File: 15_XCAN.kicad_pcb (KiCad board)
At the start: 2 copper layers, 12.1 x 17.1 mm, 5 parts, among them J1 Conn_01x06, J7 Conn_01x01, U1 MCP2551-I-SN

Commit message: maj fichiers de fabrication
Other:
- rule pad_to_mask_clearance: 0.05 -> 0
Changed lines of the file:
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@@
   )
   (setup
-    (pad_to_mask_clearance 0.05)
+    (stackup
+      (layer "F.SilkS" (type "Top Silk Screen"))
+      (layer "F.Paste" (type "Top Solder Paste"))
+      (layer "F.Mask" (type "Top Solder Mask") (thickness 0.01))
+      (layer "F.Cu" (type "copper") (thickness 0.035))
+      (layer "dielectric 1" (type "core") (thickness 1.51) (material "FR4") (epsilon_r 4.5) (loss_tangent 0.02))
+      (layer "B.Cu" (type "copper") (thickness 0.035))
+      (layer "B.Mask" (type "Bottom Solder Mask") (thickness 0.01))
+      (layer "B.Paste" (type "Bottom Solder Paste"))
+      (layer "B.SilkS" (type "Bottom Silk Screen"))
+      (copper_finish "None")
+      (dielectric_constraints no)
+    )
+    (pad_to_mask_clearance 0)
     (grid_origin 104.14 78.74)
     (pcbplotparams
       (layerselection 0x00310fc_ffffffff)
       (disableapertmacros false)
-      (usegerberextensions false)
-      (usegerberattributes true)
-      (usegerberadvancedattributes true)
+      (usegerberextensions true)
+      (usegerberattributes false)
+      (usegerberadvancedattributes false)
       (creategerberjobfile false)
       (svguseinch false)
       (svgprecision 6)
-      (excludeedgelayer false)
+      (excludeedgelayer true)
       (plotframeref false)
       (viasonmask false)
       (mode 1)
-      (useauxorigin true)
+      (useauxorigin false)
       (hpglpennumber 1)
       (hpglpenspeed 20)
@@
       (psa4output false)
       (plotreference true)
-      (plotvalue true)
+      (plotvalue false)
       (plotinvisibletext false)
       (sketchpadsonfab false)
-      (subtractmaskfromsilk false)
+      (subtractmaskfromsilk true)
       (outputformat 1)
       (mirror false)

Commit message: maj
ajout sur silk
changement sourcing jlcpcb
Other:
- board text added: "H"
- board text added: "L"
- board text added: "R"
- board text added: "T"
- board text added: "XCAN 2023/04/21"
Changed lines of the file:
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@@
+    (effects (font (size 1 1) (thickness 0.15)) (justify mirror))
+  )
+  (gr_text "XCAN\n2023/04/21" (at 111.76 71.755 270) (layer "B.SilkS")
     (effects (font (size 1 1) (thickness 0.15)) (justify mirror))
   )
@@
     (effects (font (size 1 1) (thickness 0.15)))
   )
+  (gr_text "R" (at 106.045 68.58) (layer "F.SilkS")
+    (effects (font (size 1 1) (thickness 0.15)))
+  )
+  (gr_text "L" (at 106.045 73.66) (layer "F.SilkS")
+    (effects (font (size 1 1) (thickness 0.15)))
+  )
   (gr_text "GND" (at 107.061 63.5) (layer "F.SilkS")
     (effects (font (size 1 1) (thickness 0.15)))
   )
+  (gr_text "H" (at 106.045 76.2) (layer "F.SilkS")
+    (effects (font (size 1 1) (thickness 0.15)))
+  )
+  (gr_text "T" (at 106.045 71.12) (layer "F.SilkS")
+    (effects (font (size 1 1) (thickness 0.15)))
+  )

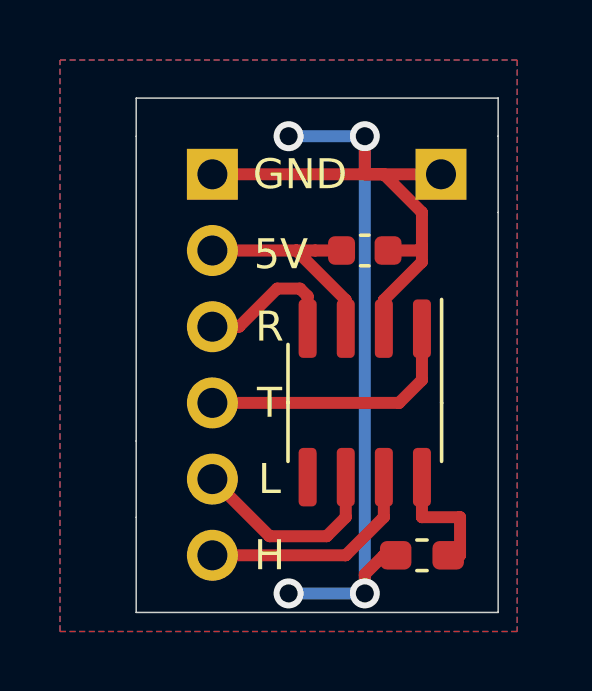
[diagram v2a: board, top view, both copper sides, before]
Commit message: version castellated holes
rajout des castellated holes
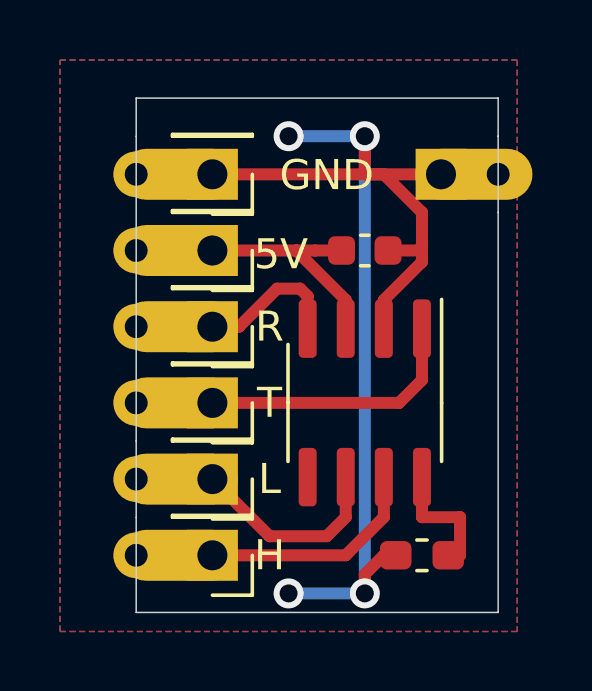
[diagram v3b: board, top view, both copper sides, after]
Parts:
- added J2: Conn_01x01, Chimere_mods:Castellated_conn, F.Cu at (104.1, 66.0)
- added J3: Conn_01x01, Chimere_mods:Castellated_conn, F.Cu at (104.1, 68.6)
- added J4: Conn_01x01, Chimere_mods:Castellated_conn, F.Cu at (104.1, 71.1)
- added J5: Conn_01x01, Chimere_mods:Castellated_conn, F.Cu at (104.1, 73.7)
- added J6: Conn_01x01, Chimere_mods:Castellated_conn, F.Cu at (104.1, 76.2)
- J1: value Conn_01x06 -> Conn_01x01; footprint Connector_PinHeader_2.54mm:PinHeader_1x06_P2.54mm_Vertical -> Chimere_mods:Castellated_conn; moved to F.Cu
- J7: footprint Connector_PinHeader_2.54mm:PinHeader_1x01_P2.54mm_Vertical -> Chimere_mods:Cast_co_1_905
- turned J7 to 0 degrees
